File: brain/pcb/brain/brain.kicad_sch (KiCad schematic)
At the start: 1 part, among them U1 Pico

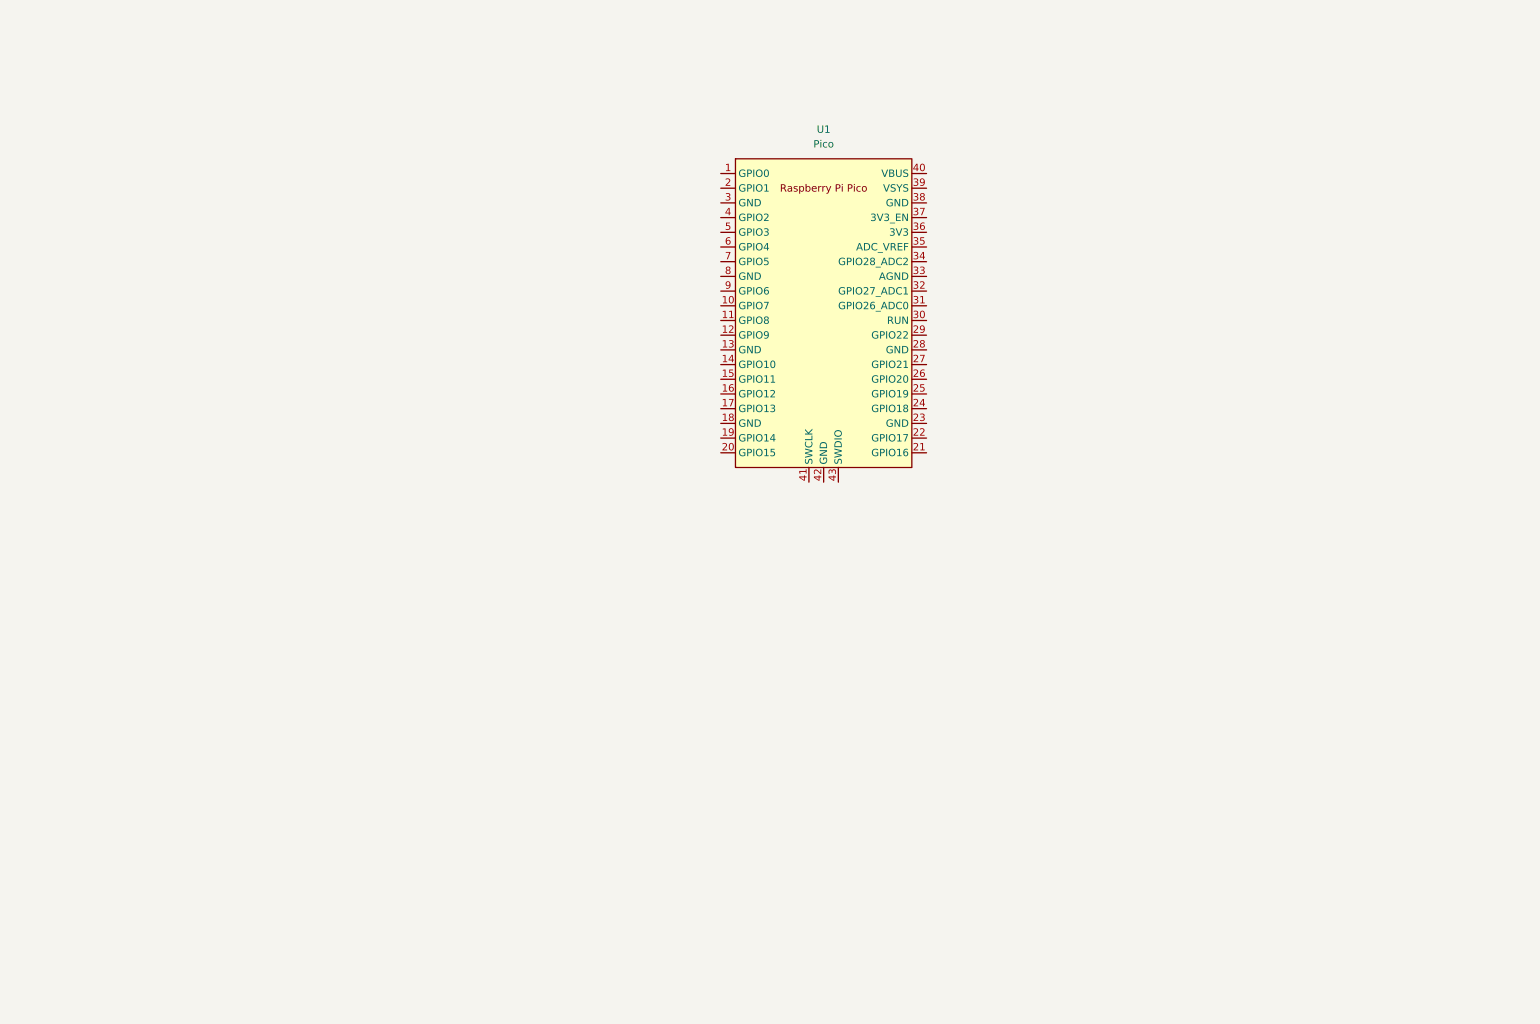
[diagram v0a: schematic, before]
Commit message: first brain schematic with sensor/motor connectors
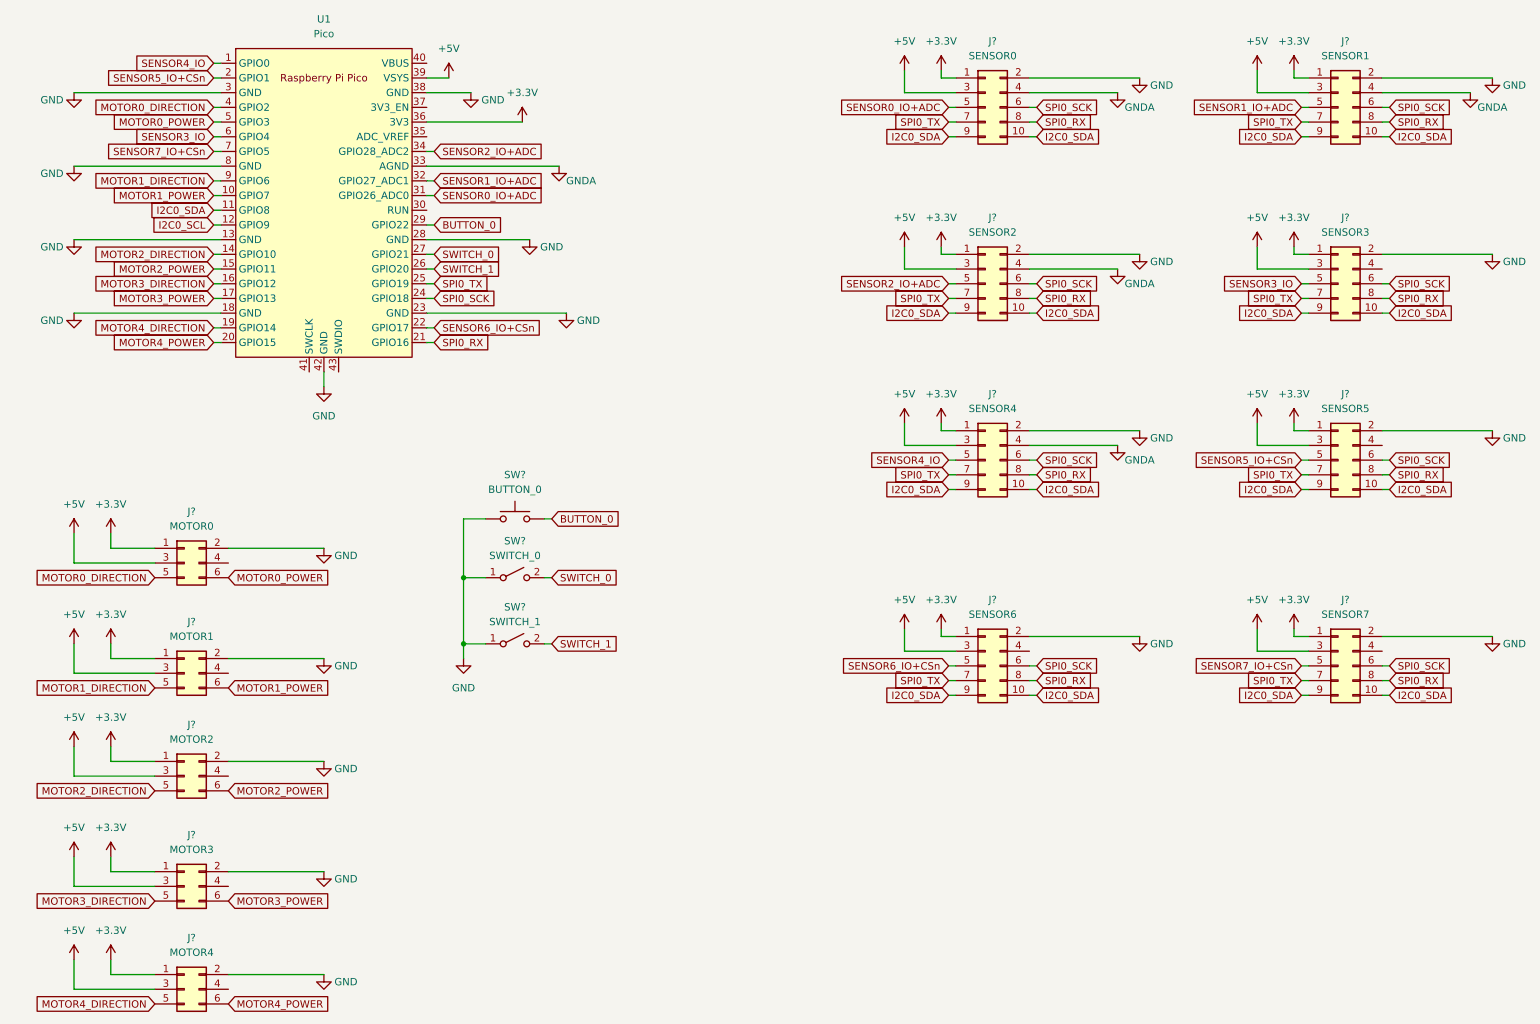
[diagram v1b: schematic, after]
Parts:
- added J?: MOTOR3, symbol Connector_Generic:Conn_02x03_Odd_Even
- added J?: SENSOR4, symbol Connector_Generic:Conn_02x05_Odd_Even
- added J?: MOTOR1, symbol Connector_Generic:Conn_02x03_Odd_Even
- added J?: SENSOR3, symbol Connector_Generic:Conn_02x05_Odd_Even
- added J?: SENSOR5, symbol Connector_Generic:Conn_02x05_Odd_Even
- added J?: SENSOR1, symbol Connector_Generic:Conn_02x05_Odd_Even
- added J?: SENSOR7, symbol Connector_Generic:Conn_02x05_Odd_Even
- added J?: SENSOR2, symbol Connector_Generic:Conn_02x05_Odd_Even
- added J?: MOTOR0, symbol Connector_Generic:Conn_02x03_Odd_Even
- added J?: SENSOR6, symbol Connector_Generic:Conn_02x05_Odd_Even
- added J?: SENSOR0, symbol Connector_Generic:Conn_02x05_Odd_Even
- added J?: MOTOR4, symbol Connector_Generic:Conn_02x03_Odd_Even
- added J?: MOTOR2, symbol Connector_Generic:Conn_02x03_Odd_Even
- added SW?: BUTTON_0, symbol Switch:SW_Push
- added SW?: SWITCH_1, symbol Switch:SW_SPST
- added SW?: SWITCH_0, symbol Switch:SW_SPST
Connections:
- net SENSOR4_IO: now reaches U1.1 (GPIO0)
- net SENSOR4_IO: now also J?.5 (Pin_5)
- net MOTOR1_POWER: now reaches U1.10 (GPIO7)
- net MOTOR1_POWER: now also J?.6 (Pin_6)
- net I2C0_SDA: now reaches U1.11 (GPIO8)
- net I2C0_SDA: now also J?.10 (Pin_10), J?.10 (Pin_10), J?.10 (Pin_10), J?.10 (Pin_10), J?.10 (Pin_10), J?.10 (Pin_10), J?.10 (Pin_10), J?.10 (Pin_10), J?.9 (Pin_9), J?.9 (Pin_9), J?.9 (Pin_9), J?.9 (Pin_9), J?.9 (Pin_9), J?.9 (Pin_9), J?.9 (Pin_9), J?.9 (Pin_9)
- net I2C0_SCL: now reaches U1.12 (GPIO9)
- net GND: now reaches U1.13 (GND)
- net GND: now also U1.18 (GND), U1.23 (GND), U1.28 (GND), U1.3 (GND), U1.38 (GND), U1.42 (GND), U1.8 (GND), J?.2 (Pin_2), J?.2 (Pin_2), J?.2 (Pin_2), J?.2 (Pin_2), J?.2 (Pin_2), J?.2 (Pin_2), J?.2 (Pin_2), J?.2 (Pin_2), J?.2 (Pin_2), J?.2 (Pin_2), J?.2 (Pin_2), J?.2 (Pin_2), J?.2 (Pin_2), SW?.1, SW?.1 (A), SW?.1 (A)
- net MOTOR2_DIRECTION: now reaches U1.14 (GPIO10)
- net MOTOR2_DIRECTION: now also J?.5 (Pin_5)
- net MOTOR2_POWER: now reaches U1.15 (GPIO11)
- net MOTOR2_POWER: now also J?.6 (Pin_6)
- net MOTOR3_DIRECTION: now reaches U1.16 (GPIO12)
- net MOTOR3_DIRECTION: now also J?.5 (Pin_5)
- net MOTOR3_POWER: now reaches U1.17 (GPIO13)
- net MOTOR3_POWER: now also J?.6 (Pin_6)
- net MOTOR4_DIRECTION: now reaches U1.19 (GPIO14)
- net MOTOR4_DIRECTION: now also J?.5 (Pin_5)
- net SENSOR5_IO+CSn: now reaches U1.2 (GPIO1)
- net SENSOR5_IO+CSn: now also J?.5 (Pin_5)
- net MOTOR4_POWER: now reaches U1.20 (GPIO15)
- net MOTOR4_POWER: now also J?.6 (Pin_6)
- net SPI0_RX: now reaches U1.21 (GPIO16)
- net SPI0_RX: now also J?.8 (Pin_8), J?.8 (Pin_8), J?.8 (Pin_8), J?.8 (Pin_8), J?.8 (Pin_8), J?.8 (Pin_8), J?.8 (Pin_8), J?.8 (Pin_8)
- net SENSOR6_IO+CSn: now reaches U1.22 (GPIO17)
- net SENSOR6_IO+CSn: now also J?.5 (Pin_5)
- net SPI0_SCK: now reaches U1.24 (GPIO18)
- net SPI0_SCK: now also J?.6 (Pin_6), J?.6 (Pin_6), J?.6 (Pin_6), J?.6 (Pin_6), J?.6 (Pin_6), J?.6 (Pin_6), J?.6 (Pin_6), J?.6 (Pin_6)
- net SPI0_TX: now reaches U1.25 (GPIO19)
- net SPI0_TX: now also J?.7 (Pin_7), J?.7 (Pin_7), J?.7 (Pin_7), J?.7 (Pin_7), J?.7 (Pin_7), J?.7 (Pin_7), J?.7 (Pin_7), J?.7 (Pin_7)
- net SWITCH_1: now reaches U1.26 (GPIO20)
- net SWITCH_1: now also SW?.2 (B)
- net SWITCH_0: now reaches U1.27 (GPIO21)
- net SWITCH_0: now also SW?.2 (B)
- net BUTTON_0: now reaches U1.29 (GPIO22)
- net BUTTON_0: now also SW?.2
- net SENSOR0_IO+ADC: now reaches U1.31 (GPIO26_ADC0)
- net SENSOR0_IO+ADC: now also J?.5 (Pin_5)
- net SENSOR1_IO+ADC: now reaches U1.32 (GPIO27_ADC1)
- net SENSOR1_IO+ADC: now also J?.5 (Pin_5)
- net GNDA: now reaches U1.33 (AGND)
- net GNDA: now also J?.4 (Pin_4), J?.4 (Pin_4), J?.4 (Pin_4), J?.4 (Pin_4)
- net SENSOR2_IO+ADC: now reaches U1.34 (GPIO28_ADC2)
- net SENSOR2_IO+ADC: now also J?.5 (Pin_5)
- net +3.3V: now reaches U1.36 (3V3)
- net +3.3V: now also J?.1 (Pin_1), J?.1 (Pin_1), J?.1 (Pin_1), J?.1 (Pin_1), J?.1 (Pin_1), J?.1 (Pin_1), J?.1 (Pin_1), J?.1 (Pin_1), J?.1 (Pin_1), J?.1 (Pin_1), J?.1 (Pin_1), J?.1 (Pin_1), J?.1 (Pin_1)
- net +5V: now reaches U1.39 (VSYS)
- net +5V: now also J?.3 (Pin_3), J?.3 (Pin_3), J?.3 (Pin_3), J?.3 (Pin_3), J?.3 (Pin_3), J?.3 (Pin_3), J?.3 (Pin_3), J?.3 (Pin_3), J?.3 (Pin_3), J?.3 (Pin_3), J?.3 (Pin_3), J?.3 (Pin_3), J?.3 (Pin_3)
- net MOTOR0_DIRECTION: now reaches U1.4 (GPIO2)
- net MOTOR0_DIRECTION: now also J?.5 (Pin_5)
- net MOTOR0_POWER: now reaches U1.5 (GPIO3)
- net MOTOR0_POWER: now also J?.6 (Pin_6)
- net SENSOR3_IO: now reaches U1.6 (GPIO4)
- net SENSOR3_IO: now also J?.5 (Pin_5)
- net SENSOR7_IO+CSn: now reaches U1.7 (GPIO5)
- net SENSOR7_IO+CSn: now also J?.5 (Pin_5)
- net MOTOR1_DIRECTION: now reaches U1.9 (GPIO6)
- net MOTOR1_DIRECTION: now also J?.5 (Pin_5)
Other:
- moved on the sheet: U1
